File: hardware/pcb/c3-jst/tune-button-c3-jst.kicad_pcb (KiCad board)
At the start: 2 copper layers, 36 x 50 mm, 40 parts, among them J1 USB-C, J2 LiPo, J3 Buttons, Q1 AO3401A, SW5 RESET, SW6 BOOT, U1 ESP32-C3-WROOM-02-N4, U2 SRV05-4, U3 TP4054, U4 RT9080-3.3, U5 SRV05-4

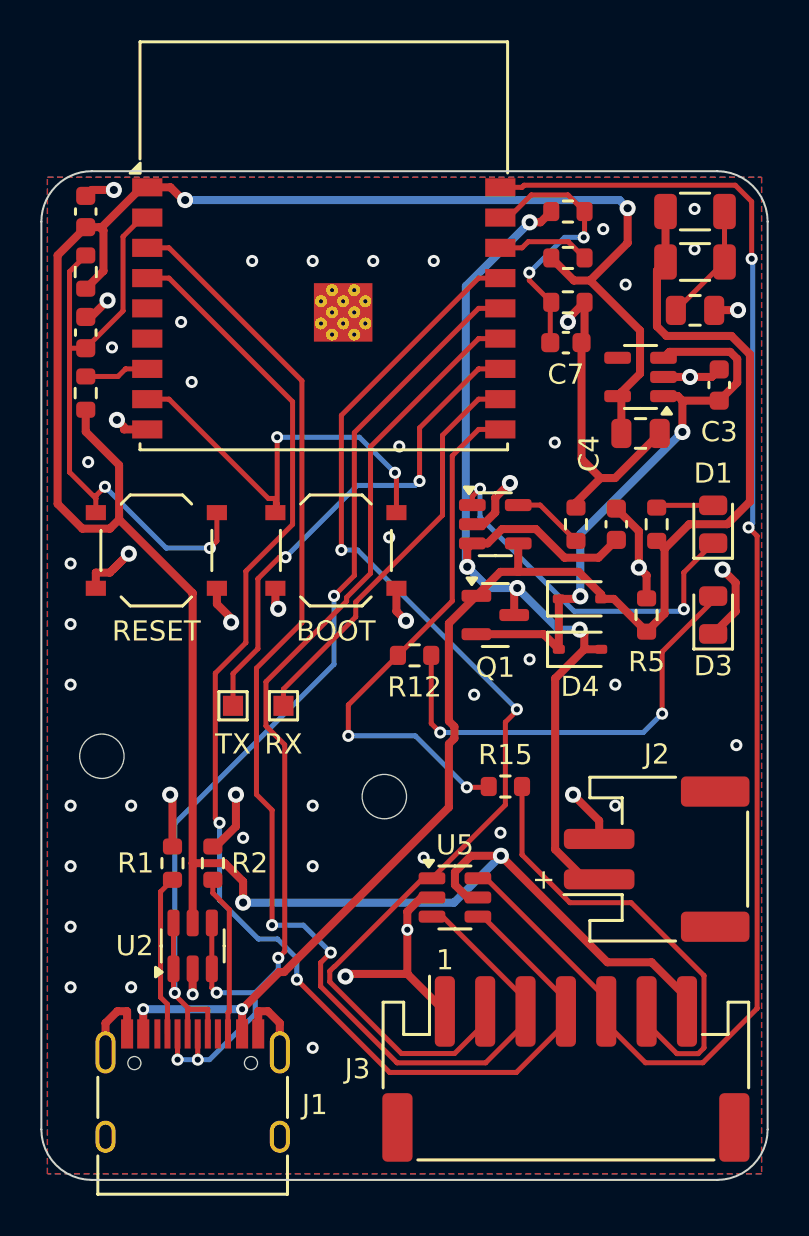
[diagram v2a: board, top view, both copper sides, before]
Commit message: pcb: c3-jst moves C1 and its damper beside the USB-C, rerouted
Up at the top right, C1 (the VBUS input capacitor) and R13/R14 were about 45 mm of track
(~36 nH) from J1. The routed-copper simulation showed a hot-plug with no cell ringing VBUS
to 9.7-11.7 V (the c3 sees 5.5-5.9 V). They now sit above J1's left VBUS pins. Placement
changed, so the board is rerouted (clean on attempt 4) and routing.json re-frozen.
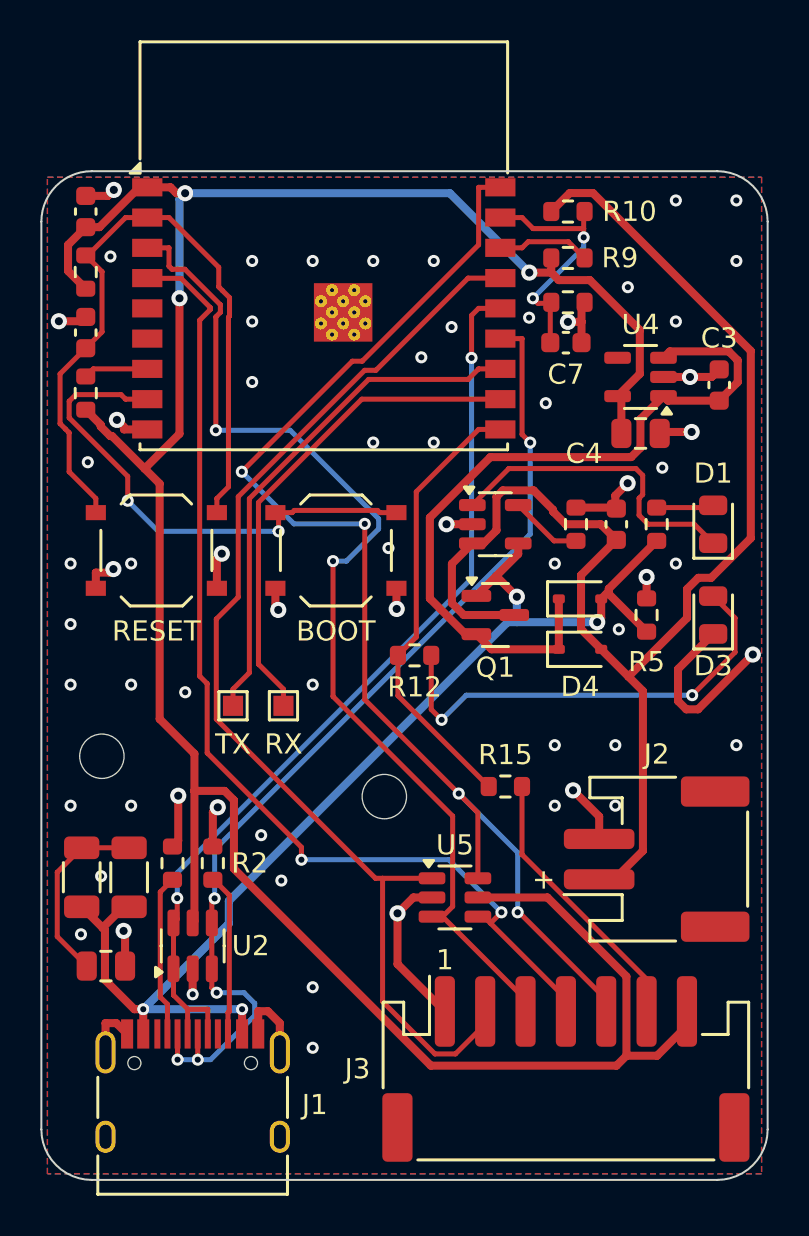
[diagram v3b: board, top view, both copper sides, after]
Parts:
- moved R13 44.9 mm to (2.00, 35.0), turned to 90 degrees
- moved C1 43.7 mm to (3.20, 39.4)
- moved R14 41.4 mm to (4.35, 35.0), turned to 90 degrees
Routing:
- net VBAT: track 52.8 -> 69.7 mm, vias 4 -> 0
- net GND: track 74.8 -> 58.3 mm, vias 54 -> 64
- net K3: track 65.7 -> 51.8 mm
- net VBUS: track 73.3 -> 60.9 mm, vias 2 -> 4
- net K2: track 64.0 -> 52.2 mm
- net K4: track 72.6 -> 61.2 mm, vias 2 -> 4
- net VSYS: track 29.0 -> 38.1 mm, vias 2 -> 0
- net LED_OUT: track 22.6 -> 13.7 mm
- net LED: track 27.0 -> 22.3 mm, vias 2 -> 0
- net RXD: track 20.3 -> 24.7 mm
- net IO9: track 21.1 -> 25.4 mm
- net EN: track 31.4 -> 35.7 mm, vias 2 -> 0
- net USB_DP: track 49.3 -> 45.8 mm
- net VBUS_C: track 5.89 -> 9.32 mm
- net STAT: track 18.3 -> 15.6 mm, vias 2 -> 0
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
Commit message: pcb: c3-jst round-8 audit fixes; panel rebuilt with the moved C1
- README: H2 now needs a nylon screw or washers (K2 and VBUS run 1.6 mm from its centre), and the
  c3-jst tab-placement remark follows the new copper.
- Back pour kept off the top edge above the 3V3 track at the antenna base (was a 0.29 mm strip).
- K4 via moved 0.1 mm off K3's (0.60 mm hole to hole).
- panel.py: no tab within 3 mm of an 0805-or-larger ceramic capacitor. Panel rebuilt: c3-jst has six
  tabs, three of them cut-not-snap.
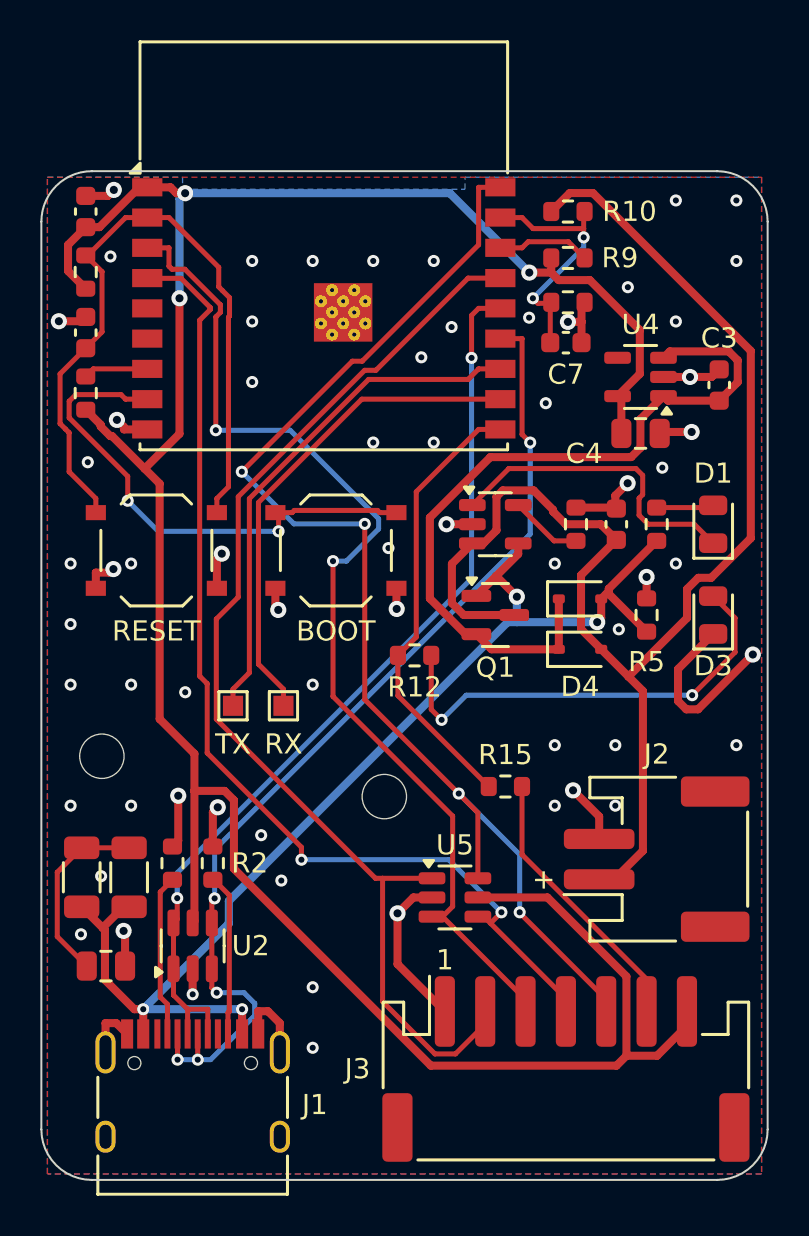
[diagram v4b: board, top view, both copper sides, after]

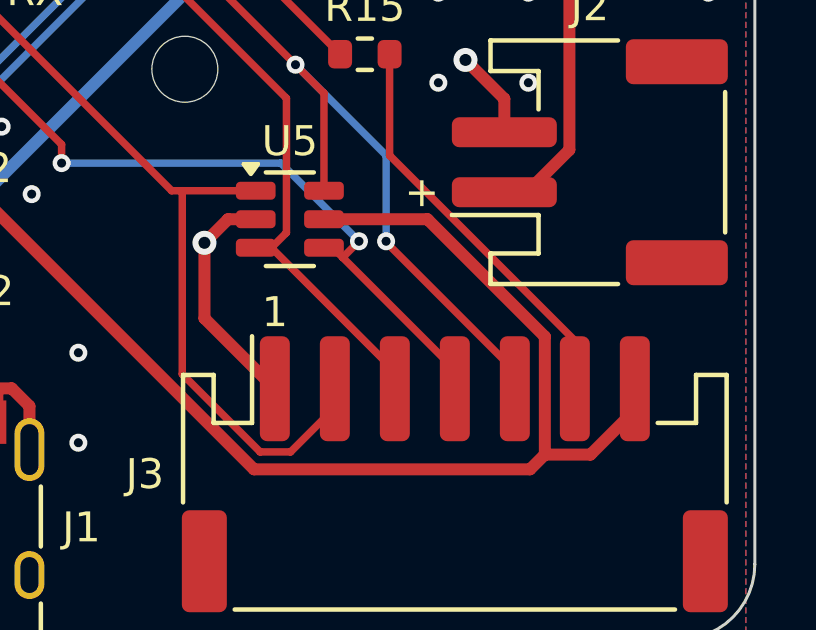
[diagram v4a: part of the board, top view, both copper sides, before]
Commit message: pcb: c3-jst round-9 audit fixes
- README: the single-board right-edge tab windows at 25-29 and 39-45 mm are inside the 2 mm
  connector keep-out, so cut those tabs rather than snapping them; H1's wording names the pour.
- K4: the 0.03 mm stub left by the via move is gone; the diagonal starts at the via, at 45 deg.
- Panel rebuilt with it.
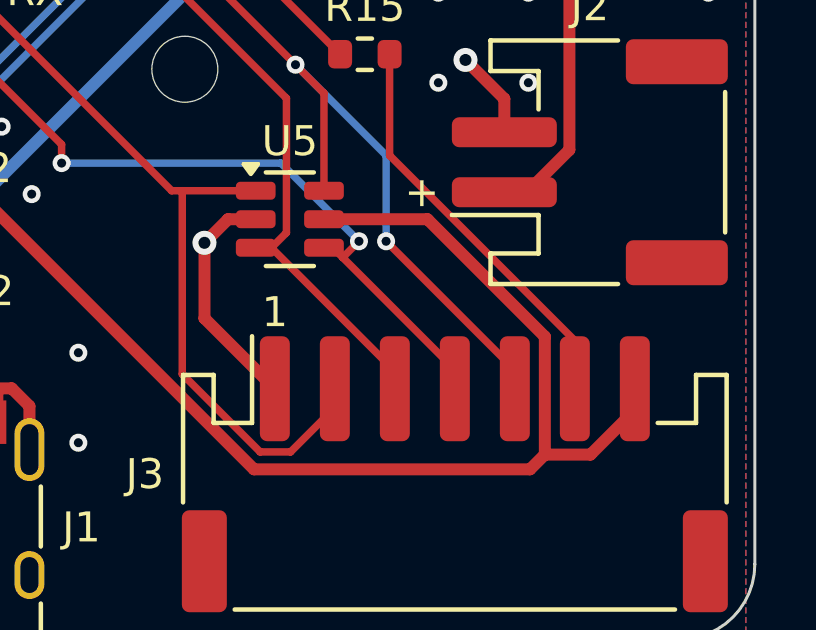
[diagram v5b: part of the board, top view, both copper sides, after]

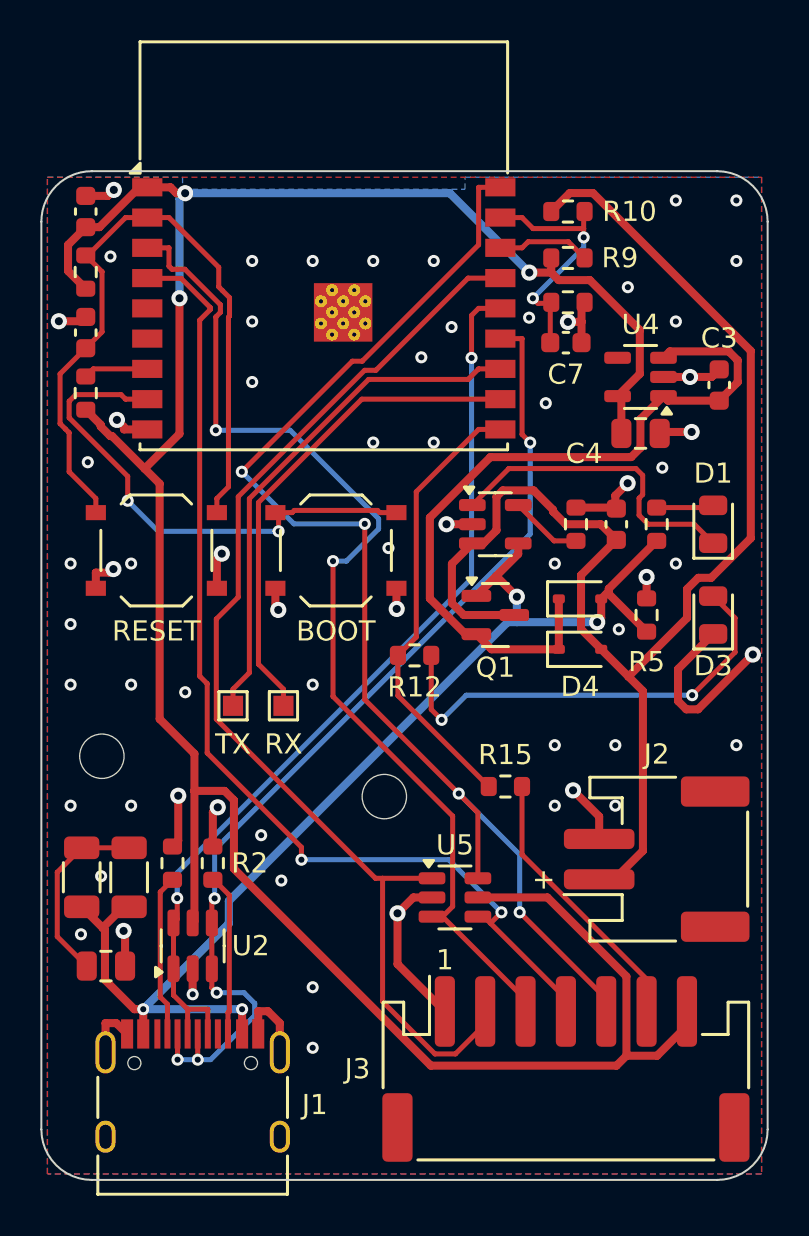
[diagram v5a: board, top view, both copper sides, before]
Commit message: pcb: c3-jst: RC damper (R16 1 ohm + C8 10 uF) at the RT9080 input, rerouted
sim12 had VSYS ringing to 6.6-6.7 V on a no-cell hot-plug against the RT9080's 6.5 V; sim13 puts
the damped worst case at 5.86 V. Panel rebuilt; README tab gaps and cutoff figures updated.
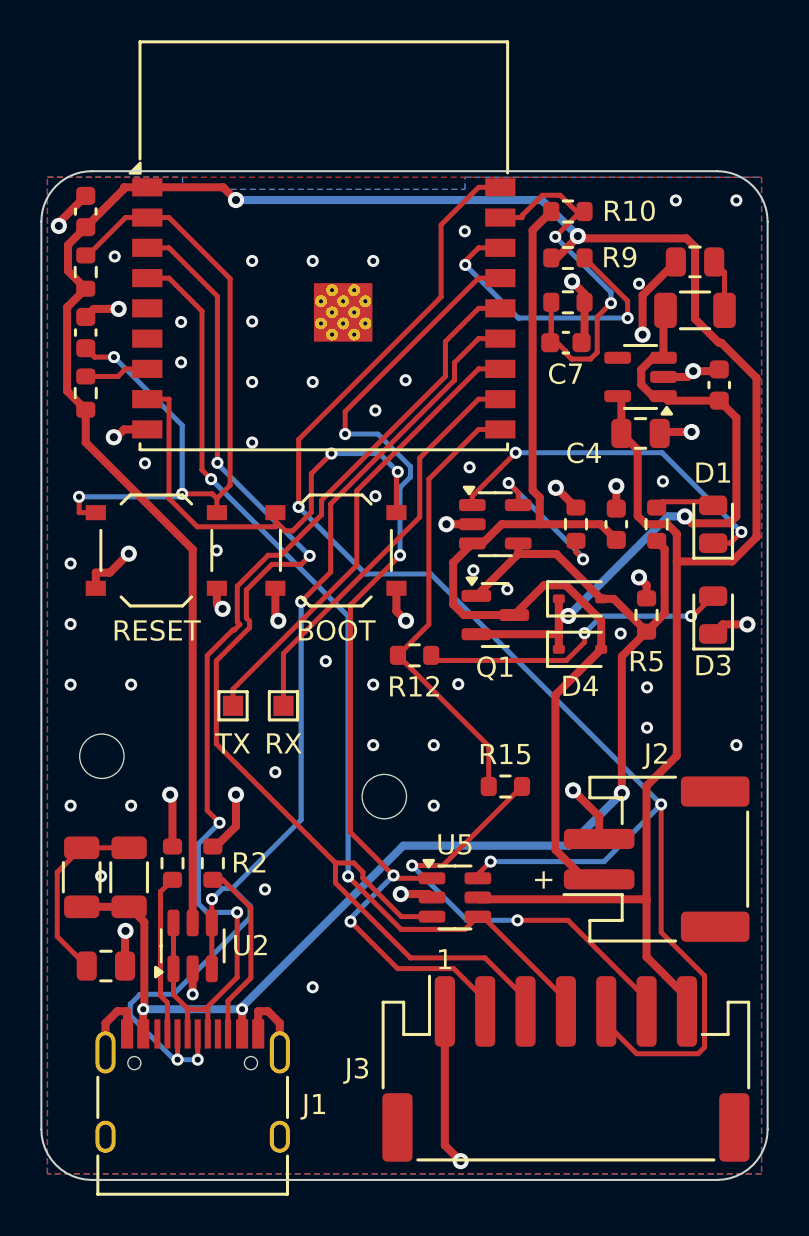
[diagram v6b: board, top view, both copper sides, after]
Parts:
- added C8: 10u, Capacitor_SMD:C_0805_2012Metric, F.Cu at (32.4, 4.50)
- added R16: 1, Resistor_SMD:R_1206_3216Metric, F.Cu at (32.4, 6.90)
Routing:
- net VBAT: track 69.7 -> 51.3 mm
- net K4: track 61.2 -> 74.6 mm, vias 4 -> 3
- net IO2: track 4.63 -> 15.2 mm, vias 0 -> 2
- net LED_OUT: track 13.7 -> 22.0 mm, vias 0 -> 2
- net USB_DP: track 45.8 -> 53.0 mm
- net K2: track 52.2 -> 59.3 mm
- net LED_A: track 22.6 -> 15.7 mm
- net VBAT_SENSE: track 12.7 -> 19.6 mm
- net VSYS: track 38.1 -> 32.5 mm, vias 0 -> 2
- net USB_DN: track 50.3 -> 55.0 mm, vias 5 -> 4
- net K1: track 56.4 -> 51.8 mm, vias 0 -> 4
- net 3V3: track 130.1 -> 134.6 mm, vias 3 -> 2
- net RXD: track 24.7 -> 20.3 mm
- net PROG: track 3.60 -> 7.66 mm, vias 0 -> 2
- net GND: track 58.3 -> 62.1 mm, vias 64 -> 66
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
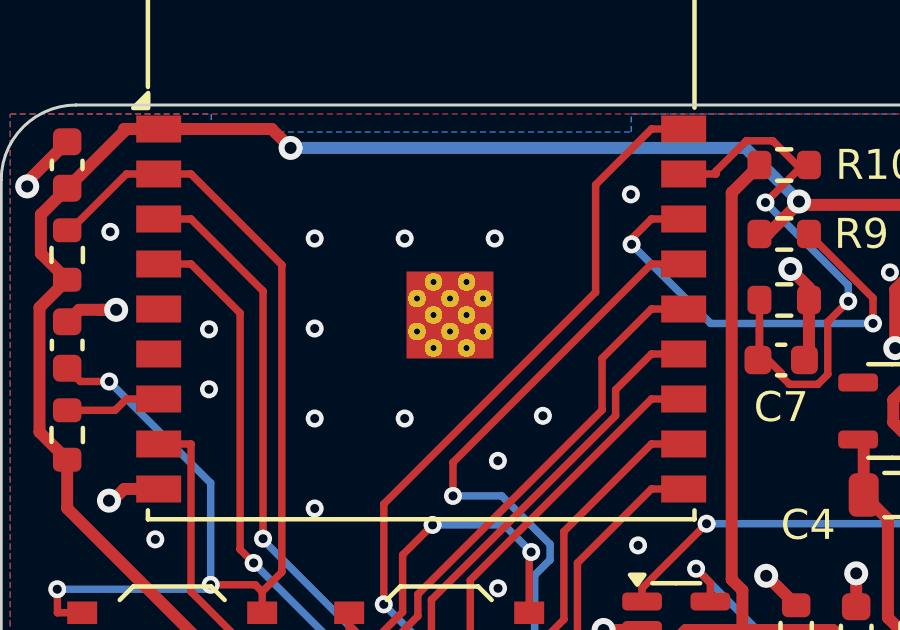
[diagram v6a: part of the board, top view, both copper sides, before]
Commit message: pcb: no hole under 0.3 mm (JLC standard): the module's 12 thermal vias go 0.2 -> 0.3 mm, DRC minimum 0.3
JLC prices 0.2 mm holes as an option: $20 -> $70 for the panel. Only those pad drills change;
copper, nets and positions are identical on all three boards.
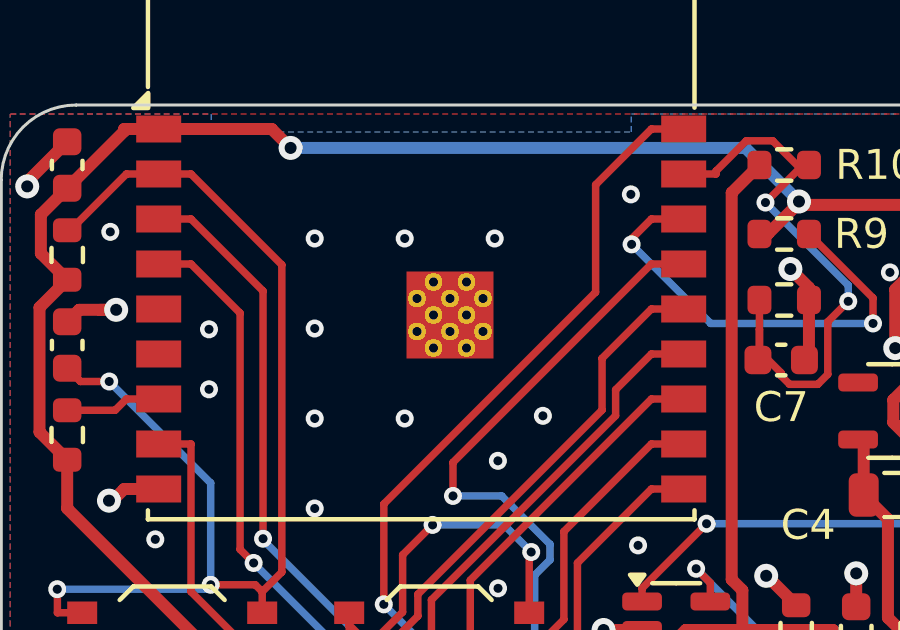
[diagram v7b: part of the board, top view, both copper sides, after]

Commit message: pcb: no JLCJLCJLCJLC order-number marker on any board (ordered with Remove Mark)
Only the marker text and its no-via rule area go; parts, copper and fills are identical, and the
BOM and CPL are unchanged. README says to choose Remove Mark.
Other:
- board text removed: "JLCJLCJLCJLC"
